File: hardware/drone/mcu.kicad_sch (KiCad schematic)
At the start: 35 parts, among them J3 USB_C_Receptacle_USB2.0_16P, J4 Conn_ARM_SWD_TagConnect_TC2030, SW1 SW_MEC_5E, U1 STM32N645I0, U20 TVS0500DRV, U6 MX25UW25645GXDI00, Y3 Crystal_GND24

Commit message: Small cleanup
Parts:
- R25, R26, R27, R28, R29: footprint BM08BSRSSTBLFSN -> (none)
- U1: footprint (none) -> STM32N645I0:BGA178C80P14X14_1200X1200X100
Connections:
- net SPK_EN: now reaches U1.C14 (PE10)
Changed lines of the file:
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@@
 	(wire
 		(pts
+			(xy 537.21 46.99) (xy 543.56 46.99)
+		)
+		(stroke
+			(width 0)
+			(type default)
+		)
+	)
+	(wire
+		(pts
 			(xy 200.66 50.8) (xy 204.47 50.8)
 		)
@@
 			3.81 3.81 3.81 3.81 3.81 3.81 3.81 3.81 3.81 3.81 3.81 3.81 3.81 3.81
 			3.81 3.81 3.81 3.81 3.81 3.81 3.81 3.81 3.81 3.81 3.81 3.81 3.81 3.81
-			3.81 3.81 3.81 3.81 3.81 3.81 3.81
+			3.81 3.81 3.81 3.81 3.81 3.81 3.81 3.81
 		)
 		(cells
@@
 				)
 			)
+			(table_cell "C14"
+				(exclude_from_sim no)
+				(at 382.905 367.665 0)
+				(size 20.32 3.81)
+				(margins 0.9525 0.9525 0.9525 0.9525)
+				(span 1 1)
+				(fill
+					(type none)
+				)
+				(effects
+					(font
+						(size 2.032 2.032)
+					)
+					(justify left top)
+				)
+			)
+			(table_cell "PE10"
+				(exclude_from_sim no)
+				(at 403.225 367.665 0)
+				(size 20.32 3.81)
+				(margins 0.9525 0.9525 0.9525 0.9525)
+				(span 1 1)
+				(fill
+					(type none)
+				)
+				(effects
+					(font
+						(size 2.032 2.032)
+					)
+					(justify left top)
+				)
+			)
+			(table_cell "GPIO (SPK_EN)"
+				(exclude_from_sim no)
+				(at 423.545 367.665 0)
+				(size 40.64 3.81)
+				(margins 0.9525 0.9525 0.9525 0.9525)
+				(span 1 1)
+				(fill
+					(type none)
+				)
+				(effects
+					(font
+						(size 2.032 2.032)
+					)
+					(justify left top)
+				)
+			)
+			(table_cell "Speaker Amp"
+				(exclude_from_sim no)
+				(at 464.185 367.665 0)
+				(size 38.1 3.81)
+				(margins 0.9525 0.9525 0.9525 0.9525)
+				(span 1 1)
+				(fill
+					(type none)
+				)
+				(effects
+					(font
+						(size 2.032 2.032)
+					)
+					(justify left top)
+				)
+			)
+			(table_cell ""
+				(exclude_from_sim no)
+				(at 502.285 367.665 0)
+				(size 38.1 3.81)
+				(margins 0.9525 0.9525 0.9525 0.9525)
+				(span 1 1)
+				(fill
+					(type none)
+				)
+				(effects
+					(font
+						(size 2.032 2.032)
+					)
+					(justify left top)
+				)
+			)
 		)
 	)
@@
 		)
 	)
+	(global_label "SPK_EN"
+		(shape input)
+		(at 543.56 46.99 0)
+		(fields_autoplaced yes)
+		(effects
+			(font
+				(size 1.27 1.27)
+			)
+			(justify left)
+		)
+		(property "Intersheetrefs" "${INTERSHEET_REFS}"
+			(at 553.7418 46.99 0)
+			(hide yes)
+			(show_name no)
+			(do_not_autoplace no)
+			(effects
+				(font
+					(size 1.27 1.27)
+				)
+				(justify left)
+			)
+		)
+	)
 	(global_label "IMU_INT1"
 		(shape input)
@@
 			)
 		)
-		(property "Footprint" "BM08BSRSSTBLFSN"
+		(property "Footprint" ""
 			(at 202.438 57.15 90)
 			(hide yes)
@@
 			)
 		)
-		(property "Footprint" ""
+		(property "Footprint" "STM32N645I0:BGA178C80P14X14_1200X1200X100"
 			(at 55.88 54.61 0)
 			(hide yes)
@@
 			)
 		)
-		(property "Footprint" "BM08BSRSSTBLFSN"
+		(property "Footprint" ""
 			(at 219.71 52.578 90)
 			(hide yes)
@@
 			)
 		)
-		(property "Footprint" ""
+		(property "Footprint" "STM32N645I0:BGA178C80P14X14_1200X1200X100"
 			(at 448.31 54.61 0)
 			(hide yes)
@@
 			)
 		)
-		(property "Footprint" ""
+		(property "Footprint" "STM32N645I0:BGA178C80P14X14_1200X1200X100"
 			(at 173.99 209.55 0)
 			(hide yes)
@@
 			)
 		)
-		(property "Footprint" ""
+		(property "Footprint" "STM32N645I0:BGA178C80P14X14_1200X1200X100"
 			(at 419.1 101.6 0)
 			(hide yes)
@@
 			)
 		)
-		(property "Footprint" ""
+		(property "Footprint" "STM32N645I0:BGA178C80P14X14_1200X1200X100"
 			(at 327.66 46.99 0)
 			(hide yes)
@@
 			)
 		)
-		(property "Footprint" ""
+		(property "Footprint" "STM32N645I0:BGA178C80P14X14_1200X1200X100"
 			(at 520.7 53.34 0)
 			(hide yes)
@@
 			)
 		)
-		(property "Footprint" "BM08BSRSSTBLFSN"
+		(property "Footprint" ""
 			(at 306.07 187.198 90)
 			(hide yes)
@@
 			)
 		)
-		(property "Footprint" ""
+		(property "Footprint" "STM32N645I0:BGA178C80P14X14_1200X1200X100"
 			(at 152.4 50.8 0)
 			(hide yes)
@@
 			)
 		)
-		(property "Footprint" "BM08BSRSSTBLFSN"
+		(property "Footprint" ""
 			(at 306.07 189.738 90)
 			(hide yes)
@@
 			)
 		)
-		(property "Footprint" ""
+		(property "Footprint" "STM32N645I0:BGA178C80P14X14_1200X1200X100"
 			(at 196.85 97.79 0)
 			(hide yes)
@@
 			)
 		)
-		(property "Footprint" ""
+		(property "Footprint" "STM32N645I0:BGA178C80P14X14_1200X1200X100"
 			(at 320.04 92.71 0)
 			(hide yes)
@@
 			)
 		)
-		(property "Footprint" "BM08BSRSSTBLFSN"
+		(property "Footprint" ""
 			(at 208.28 52.578 90)
 			(hide yes)
@@
 			)
 		)
-		(property "Footprint" ""
+		(property "Footprint" "STM32N645I0:BGA178C80P14X14_1200X1200X100"
 			(at 120.65 115.57 0)
 			(hide yes)
@@
 			)
 		)
-		(property "Footprint" ""
+		(property "Footprint" "STM32N645I0:BGA178C80P14X14_1200X1200X100"
 			(at 237.49 210.82 0)
 			(hide yes)

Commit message: Small cleanup and pinmuxxed OSPI_NRESET
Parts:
- added D5: BAT60JFILM, symbol Device:D_Schottky
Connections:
- net OSPI_NRESET: now reaches U1.J12 (PN12)
- net OSPI_NRESET: now also D5.1 (K)
- net at R7.1, U6.A4 (~{RESET}): now also D5.2 (A)
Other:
- moved on the sheet: C29, C30, C31, C32, C33, C34, C93, C94, D3, D4, J3, R13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

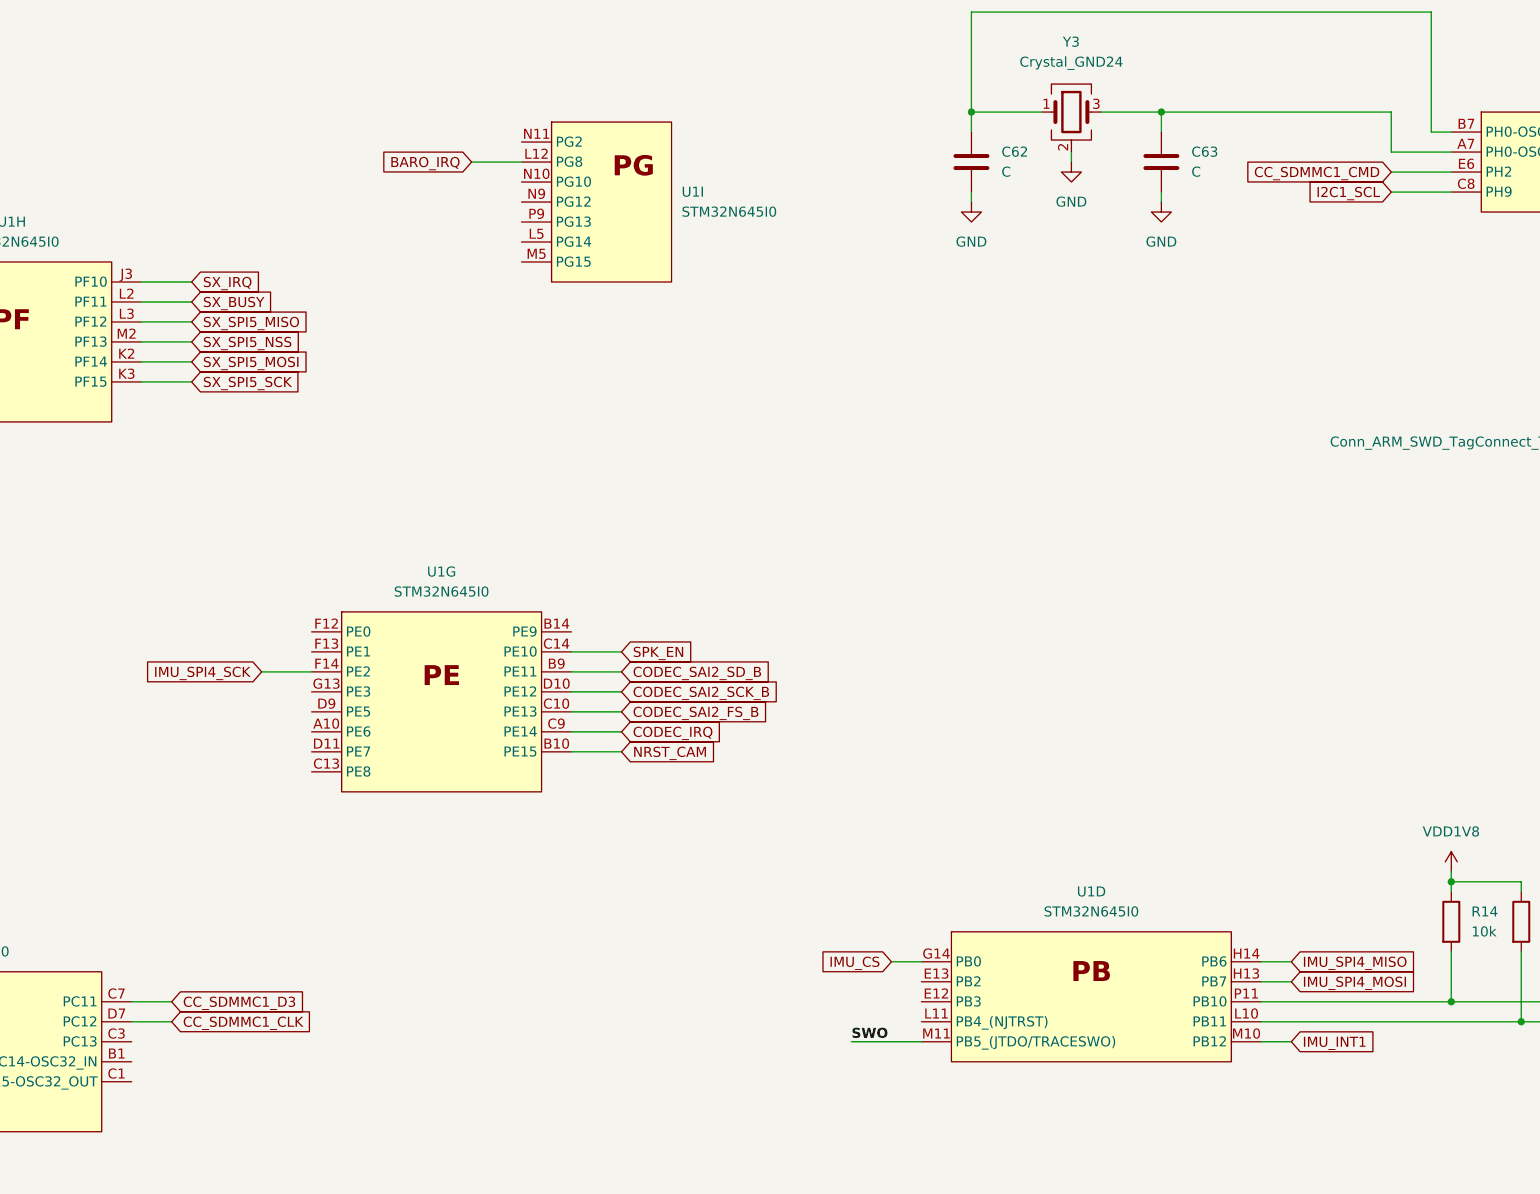
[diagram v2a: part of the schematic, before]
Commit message: Fixed some pullups and pinmuxxed more
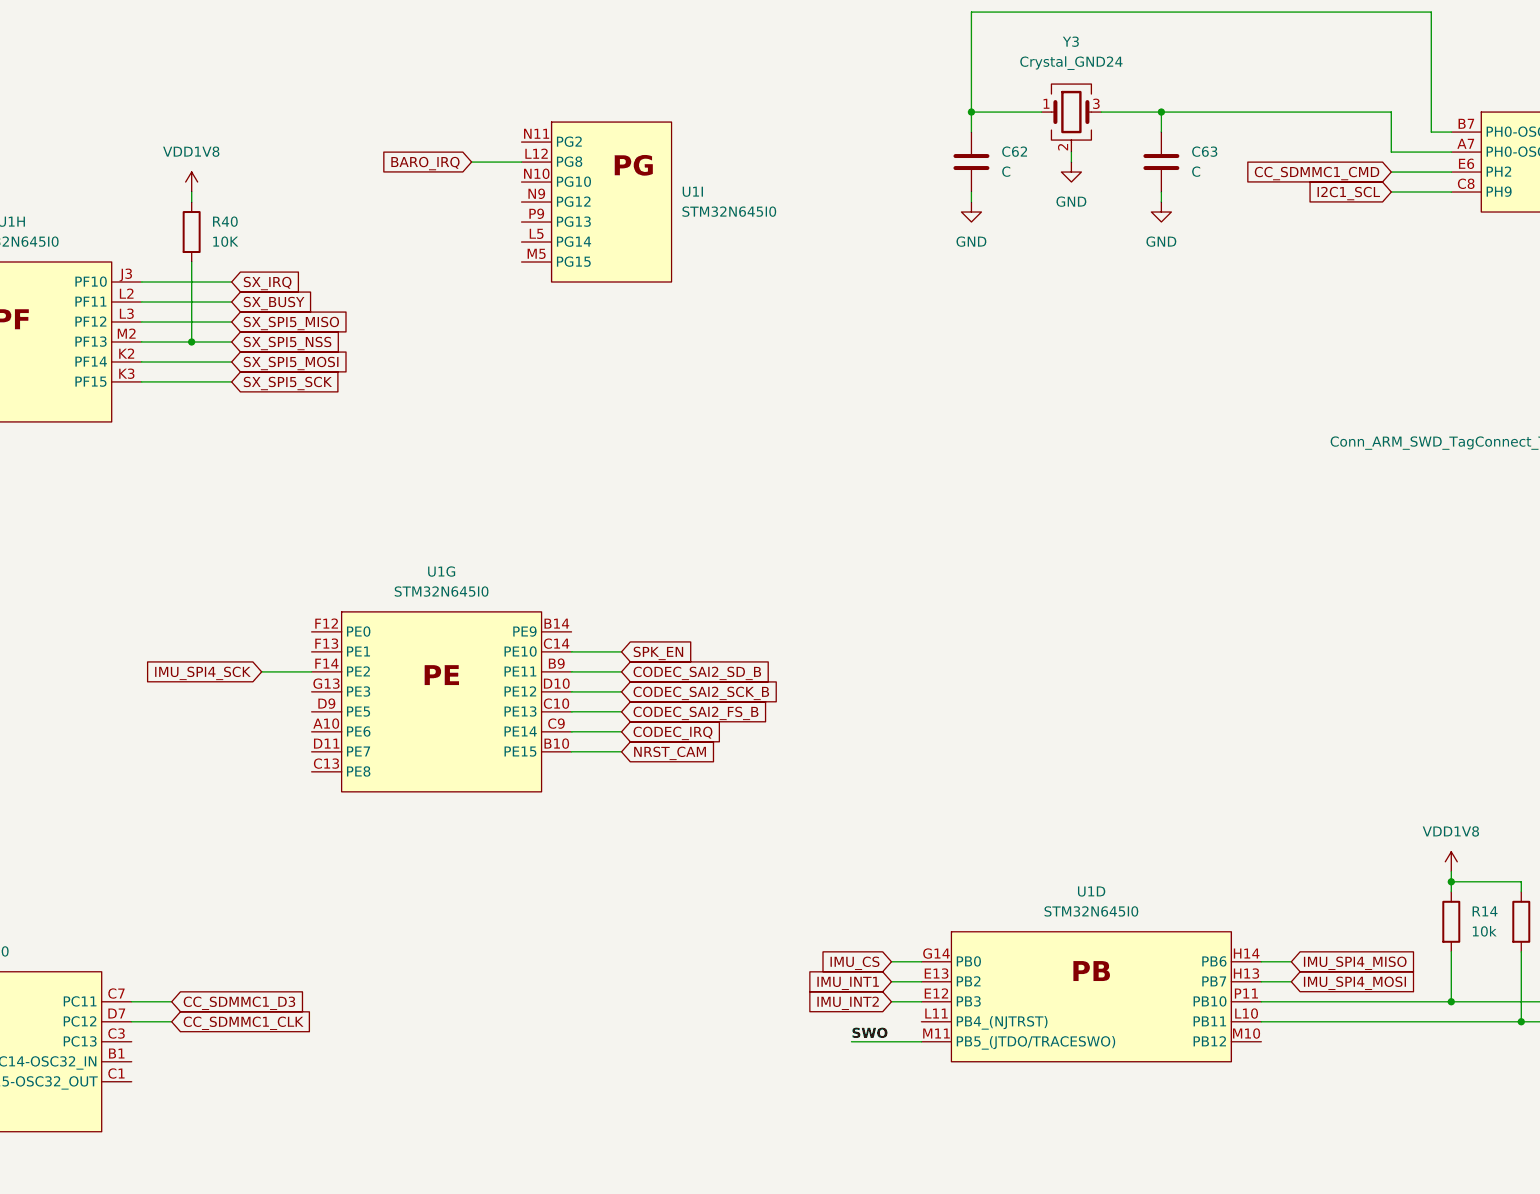
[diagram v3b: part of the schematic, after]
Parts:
- added R40: 10K, symbol Device:R
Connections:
- net IMU_INT1: now also U1.E13 (PB2); no longer U1.M10 (PB12)
- net SX_SPI5_NSS: now also R40.2
- net VDD1V8: now also R40.1
- net IMU_INT2: now reaches U1.E12 (PB3)

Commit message: Fixed i2c pullups
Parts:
- added C122, C58: C, symbol Device:C
- added R43, R44: 2.2k, symbol Device:R
- added Y4: Crystal, symbol Device:Crystal
- R13, R14: value 10k -> 2.2k
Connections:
- net GND: now also C122.2, C58.2
- net I2C1_SCL: now also R43.2
- net I2C1_SDA: now also R44.2
- net VDD1V8: now also R43.1, R44.1
- net at U1.B1 (PC14-OSC32_IN): now also C58.1, Y4.2
- net at U1.C1 (PC15-OSC32_OUT): now also C122.1, Y4.1

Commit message: Started footprint assignments
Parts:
- D3, D4: footprint Package_DIP:DIP-40_W15.24mm -> (none)
- SW1: footprint Button_Switch_SMD:SW_SPST_CK_KMS2xxGP -> (none)
- U6: footprint (none) -> MX25UW25645GXDI00:BGA24C100P5X5_600X800X120
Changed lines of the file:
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@@
 			)
 		)
-		(property "Footprint" "Package_DIP:DIP-40_W15.24mm"
+		(property "Footprint" ""
 			(at 294.64 317.5 0)
 			(hide yes)
@@
 			)
 		)
-		(property "Footprint" "Package_DIP:DIP-40_W15.24mm"
+		(property "Footprint" ""
 			(at 309.88 317.5 0)
 			(hide yes)
@@
 			)
 		)
-		(property "Footprint" "Button_Switch_SMD:SW_SPST_CK_KMS2xxGP"
+		(property "Footprint" ""
 			(at 97.79 64.77 0)
 			(hide yes)
@@
 			)
 		)
-		(property "Footprint" ""
+		(property "Footprint" "MX25UW25645GXDI00:BGA24C100P5X5_600X800X120"
 			(at 99.06 314.96 0)
 			(hide yes)

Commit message: Continued footprint assignments
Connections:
- net GNSS_TIMEPULSE renamed GNSS_TIM_1V8
- no-connect marks 8 -> 48
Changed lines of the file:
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@@
+	)
+	(no_connect
+		(at 135.89 204.47)
+	)
+	(no_connect
+		(at 158.75 152.4)
+	)
+	(no_connect
+		(at 118.11 166.37)
+	)
+	(no_connect
+		(at 104.14 113.03)
+	)
+	(no_connect
+		(at 118.11 156.21)
+	)
+	(no_connect
+		(at 130.81 53.34)
 	)
 	(no_connect
@@
 	)
 	(no_connect
+		(at 118.11 168.91)
+	)
+	(no_connect
+		(at 185.42 100.33)
+	)
+	(no_connect
+		(at 236.22 201.93)
+	)
+	(no_connect
+		(at 87.63 168.91)
+	)
+	(no_connect
+		(at 191.77 152.4)
+	)
+	(no_connect
 		(at 264.16 327.66)
 	)
 	(no_connect
+		(at 158.75 170.18)
+	)
+	(no_connect
+		(at 185.42 105.41)
+	)
+	(no_connect
+		(at 130.81 58.42)
+	)
+	(no_connect
+		(at 158.75 154.94)
+	)
+	(no_connect
+		(at 104.14 107.95)
+	)
+	(no_connect
+		(at 173.99 58.42)
+	)
+	(no_connect
+		(at 185.42 102.87)
+	)
+	(no_connect
+		(at 130.81 43.18)
+	)
+	(no_connect
 		(at 264.16 339.09)
 	)
 	(no_connect
+		(at 185.42 90.17)
+	)
+	(no_connect
+		(at 118.11 153.67)
+	)
+	(no_connect
+		(at 118.11 158.75)
+	)
+	(no_connect
+		(at 87.63 163.83)
+	)
+	(no_connect
+		(at 185.42 97.79)
+	)
+	(no_connect
+		(at 158.75 165.1)
+	)
+	(no_connect
+		(at 279.4 204.47)
+	)
+	(no_connect
+		(at 130.81 48.26)
+	)
+	(no_connect
 		(at 330.2 318.77)
 	)
 	(no_connect
+		(at 118.11 171.45)
+	)
+	(no_connect
+		(at 87.63 166.37)
+	)
+	(no_connect
 		(at 330.2 321.31)
 	)
 	(no_connect
+		(at 118.11 161.29)
+	)
+	(no_connect
 		(at 264.16 341.63)
 	)
 	(no_connect
+		(at 130.81 50.8)
+	)
+	(no_connect
 		(at 264.16 300.99)
 	)
 	(no_connect
+		(at 104.14 110.49)
+	)
+	(no_connect
+		(at 158.75 160.02)
+	)
+	(no_connect
+		(at 104.14 118.11)
+	)
+	(no_connect
+		(at 118.11 163.83)
+	)
+	(no_connect
+		(at 158.75 162.56)
+	)
+	(no_connect
+		(at 196.85 317.5)
+	)
+	(no_connect
+		(at 185.42 95.25)
+	)
+	(no_connect
 		(at 264.16 320.04)
+	)
+	(no_connect
+		(at 104.14 120.65)
+	)
+	(no_connect
+		(at 158.75 167.64)
 	)
 	(wire
@@
 		)
 	)
-	(global_label "GNSS_TIMEPULSE"
+	(global_label "GNSS_TIM_1V8"
 		(shape input)
 		(at 82.55 158.75 180)
@@
 		)
 		(property "Intersheetrefs" "${INTERSHEET_REFS}"
-			(at 63.4178 158.75 0)
+			(at 66.0787 158.75 0)
 			(hide yes)
 			(show_name no)

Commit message: More footprints
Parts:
- C32, C33, C34: footprint (none) -> Capacitor_SMD:C_0402_1005Metric
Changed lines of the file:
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@@
 			)
 		)
-		(property "Footprint" ""
+		(property "Footprint" "Capacitor_SMD:C_0402_1005Metric"
 			(at 134.9248 280.67 0)
 			(hide yes)
@@
 			)
 		)
-		(property "Footprint" ""
+		(property "Footprint" "Capacitor_SMD:C_0402_1005Metric"
 			(at 123.4948 280.67 0)
 			(hide yes)
@@
 			)
 		)
-		(property "Footprint" ""
+		(property "Footprint" "Capacitor_SMD:C_0402_1005Metric"
 			(at 112.0648 280.67 0)
 			(hide yes)
